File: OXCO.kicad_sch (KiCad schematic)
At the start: 18 parts, among them U4 LT1963AEQ, U7 ADR4540

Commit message: OCXO Rev. 0
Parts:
- added 2V1: TEST_VADJ, TestPoint:TestPoint_2Pads_Pitch2.54mm_Drill0.8mm, symbol Connector:TestPoint_2Pole
- added RV1: 2K, symbol Device:R_Potentiometer_Trim
- RN1: value R_Pack04 -> 1K 0.1% ±15ppm
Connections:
- net +5V: now also C15.1, C16.1, U5.5 (Vcc)
- net GND: now also C14.2, RN1.4 (R4.1), 2V1.2
- net Vadj: now also 2V1.1, RV1.2
- net at C11.1, C13.1, U7.6 (OUT): now also RN1.8 (R1.2)
- net at RN1.1 (R1.1): now also RN1.2 (R2.1)
- net at RN1.3 (R3.1): now also RV1.3
- net at RN1.5 (R4.2): now also RN1.6 (R3.2)
- net at RN1.7 (R2.2): now also RV1.1
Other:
- note added: "1.365V"
- note added: "3.000V"
- note added: "4.096V"
- note added: "ADR4540BRZ 2ppm/°C"
- note added: "ADR4540BRZ 4ppm/°C"
- note added: "OSC5AB02"
- moved on the sheet: 5V1, C1, C14, C15, C16, C2, D2, R1, R2, R3, U4, U5

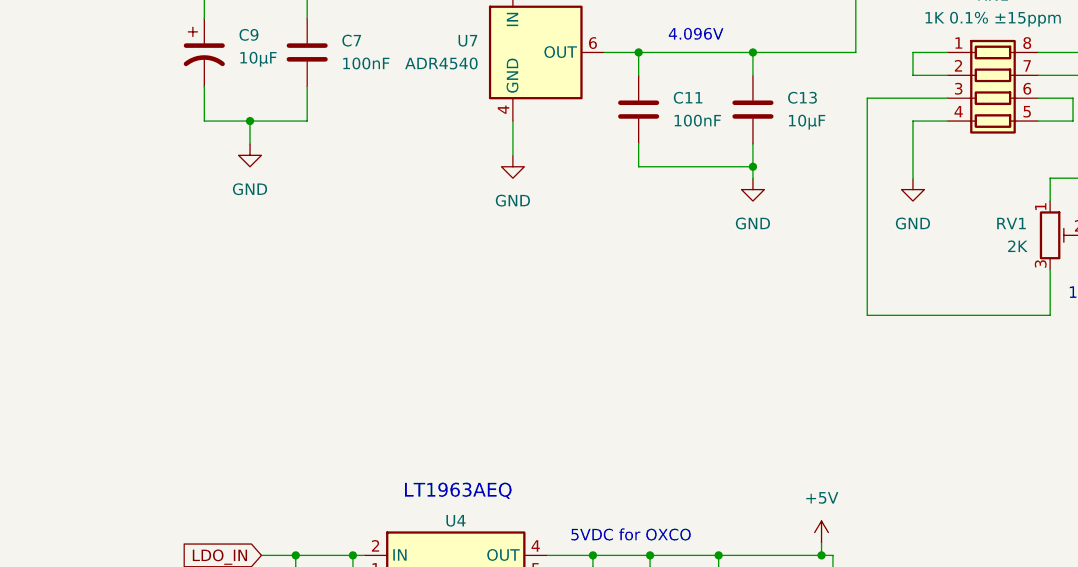
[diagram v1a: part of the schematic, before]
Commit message: Update OXCO.kicad_sch
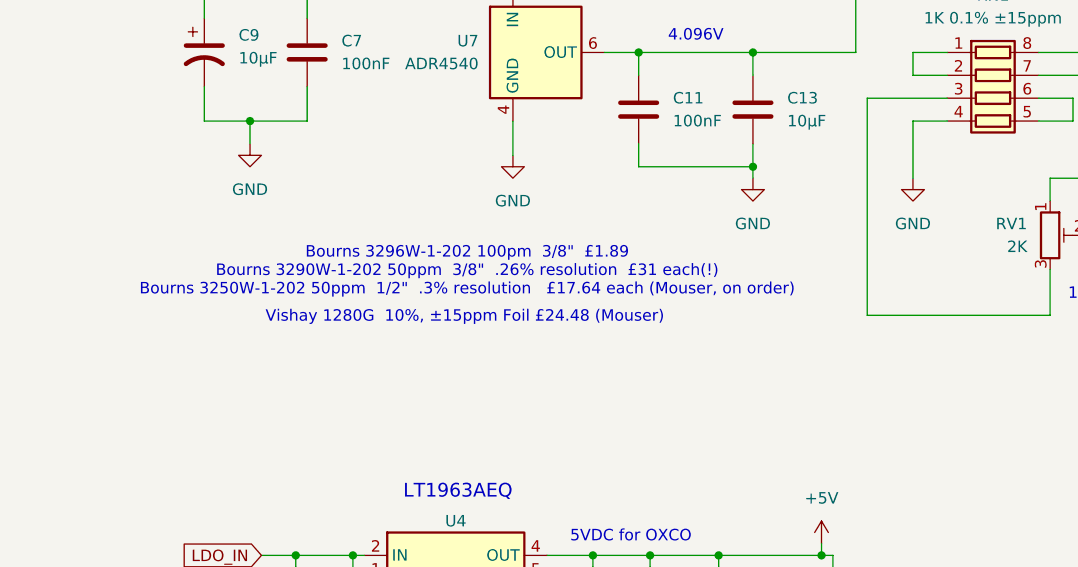
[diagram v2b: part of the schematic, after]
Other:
- note added: "Bourns 3296W-1-202 100pm 3/8" £1.89 Bourns 3290W-1-202 50ppm 3/8" .26% resolution £31 each(!) Bourns 3250W-1-202 50ppm 1/2" .3% resolution £17.64 each (Mouser, on order)"
- note added: "Vishay 1280G 10%, ±15ppm Foil £24.48 (Mouser)"
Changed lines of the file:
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@@
+		)
+	)
+	(text "Bourns 3296W-1-202 100pm  3/8\"  £1.89\nBourns 3290W-1-202 50ppm  3/8\"  .26% resolution  £31 each(!)\nBourns 3250W-1-202 50ppm  1/2\"  .3% resolution   £17.64 each (Mouser, on order)\n"
+		(exclude_from_sim no)
+		(at 60.96 94.234 0)
+		(effects
+			(font
+				(face "Arial")
+				(size 1.27 1.27)
+			)
 		)
 	)
@@
 		(effects
 			(font
+				(size 1.27 1.27)
+			)
+		)
+	)
+	(text "Vishay 1280G  10%, ±15ppm Foil £24.48 (Mouser) "
+		(exclude_from_sim no)
+		(at 60.706 99.314 0)
+		(effects
+			(font

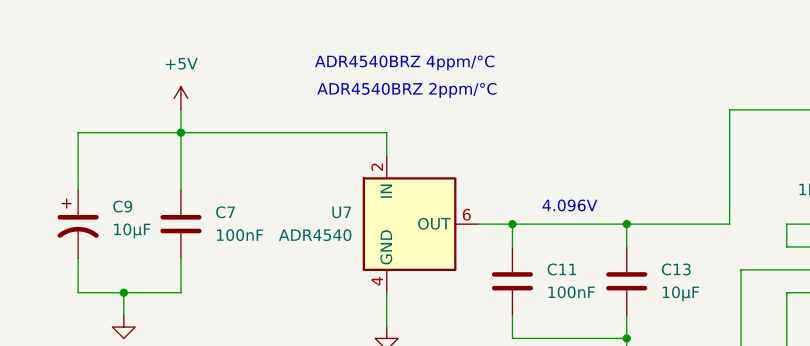
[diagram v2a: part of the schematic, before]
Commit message: Placeholder footprint for trimpot
also fix a typo
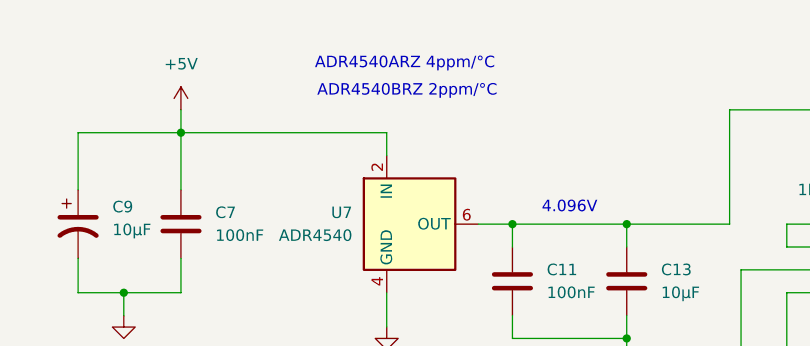
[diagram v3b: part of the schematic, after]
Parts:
- RV1: footprint (none) -> Potentiometer_THT:Potentiometer_Bourns_3296W_Vertical
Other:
- note added: "ADR4540ARZ 4ppm/°C"
- note removed: "ADR4540BRZ 4ppm/°C"
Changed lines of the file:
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@@
 		)
 	)
-	(text "ADR4540BRZ 4ppm/°C"
+	(text "ADR4540ARZ 4ppm/°C"
 		(exclude_from_sim no)
 		(at 68.072 52.07 0)
@@
 			)
 		)
-		(property "Footprint" ""
+		(property "Footprint" "Potentiometer_THT:Potentiometer_Bourns_3296W_Vertical"
 			(at 125.73 90.17 0)
 			(effects

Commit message: Add missing footprints
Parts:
- RN1: footprint (none) -> Resistor_SMD:R_Array_Convex_4x0612
- U5: footprint (none) -> Oscilator_Local:OSC5A2B02
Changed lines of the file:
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@@
 			)
 		)
-		(property "Footprint" ""
+		(property "Footprint" "Oscilator_Local:OSC5A2B02"
 			(at 194.31 63.5 0)
 			(effects
@@
 			)
 		)
-		(property "Footprint" ""
+		(property "Footprint" "Resistor_SMD:R_Array_Convex_4x0612"
 			(at 119.38 81.915 90)
 			(effects

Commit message: things
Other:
- note added: "Vishay 1280G has similar footprint as Bourn 3005P and 3006P. Possible to layout so all three fit. Be sure to import 3D files for all 3."
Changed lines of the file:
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@@
+		)
+	)
+	(text "Vishay 1280G has similar footprint as Bourn 3005P and 3006P.\nPossible to layout so all three fit.   Be sure to import 3D files for all 3.  "
+		(exclude_from_sim no)
+		(at 122.682 102.616 0)
+		(effects
+			(font
+				(size 1.27 1.27)
+			)
 		)
 	)

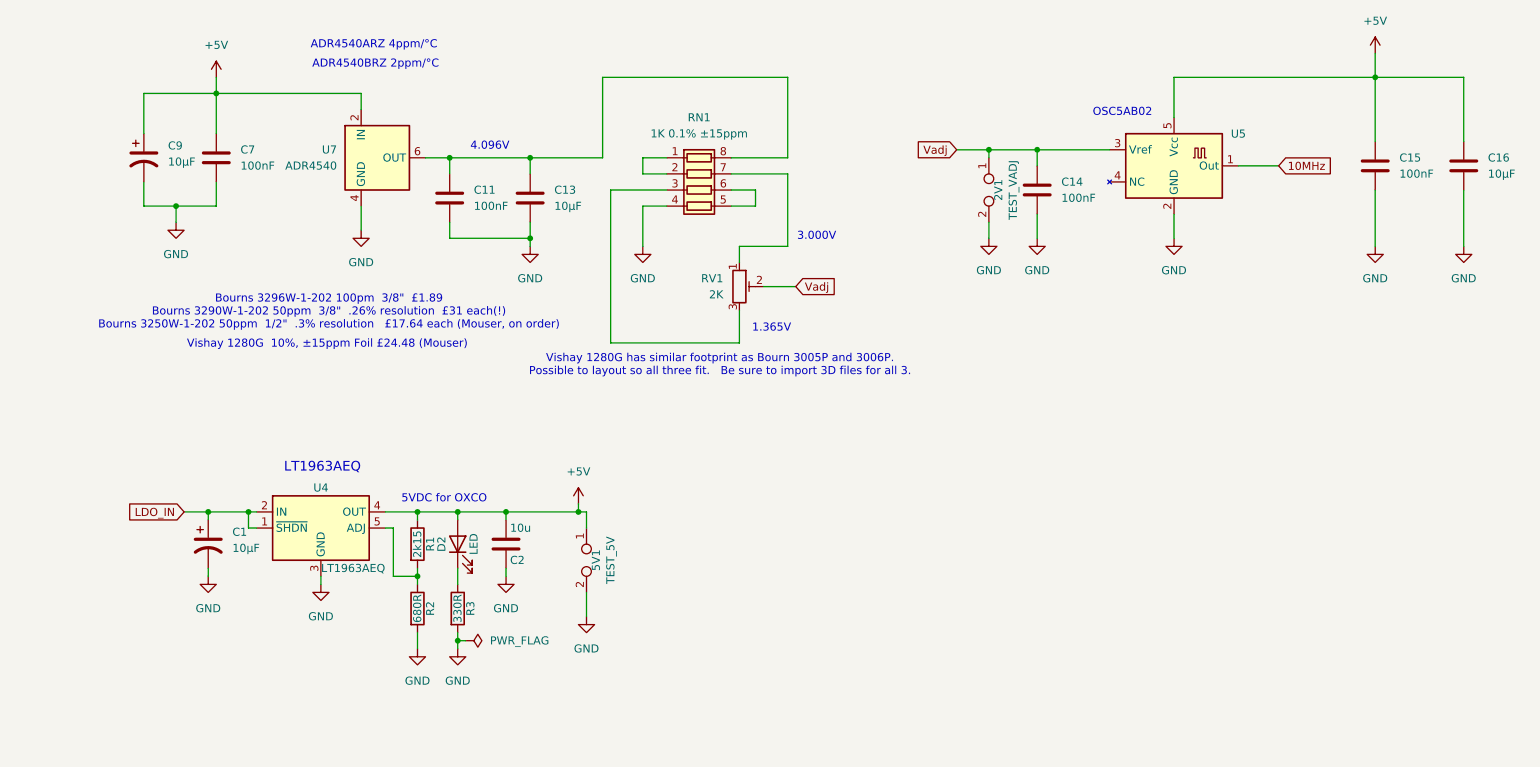
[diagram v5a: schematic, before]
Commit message: A bit of layout work
Remove sine to square parts from layout.  We don't need it.
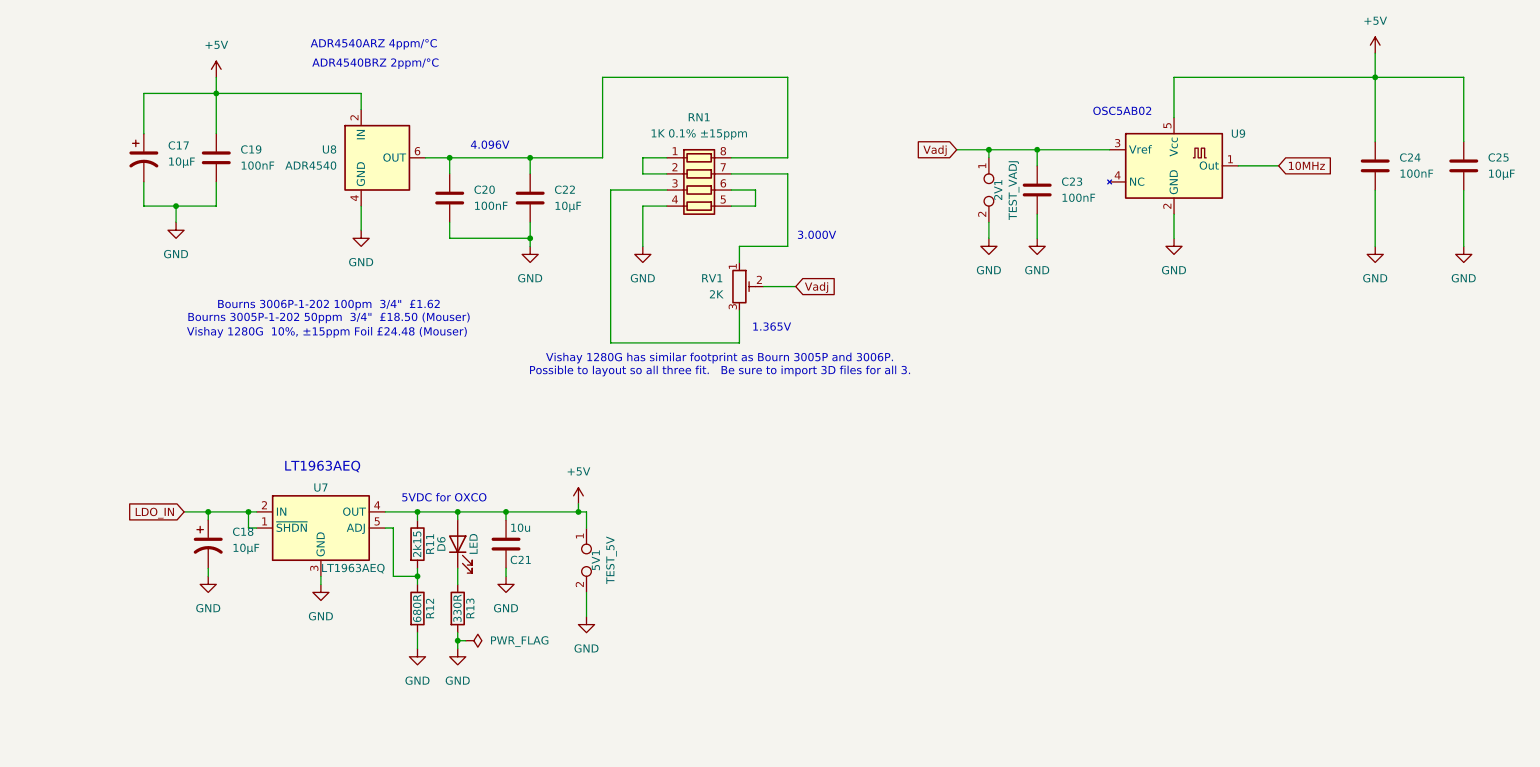
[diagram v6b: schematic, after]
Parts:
- RV1: footprint Potentiometer_THT:Potentiometer_Bourns_3296W_Vertical -> Potentiometer_THT:Potentiometer_Bourns_3006P_Horizontal; MPN (none) -> 3006P-1-202LF; RS (none) -> 521-9085
- renumbered C9 to C17, C1 to C18, C7 to C19, C11 to C20, C2 to C21, C13 to C22, C14 to C23, C15 to C24, C16 to C25, D2 to D6, R1 to R11, R2 to R12, R3 to R13, U4 to U7, U7 to U8, U5 to U9
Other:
- note added: "Bourns 3006P-1-202 100pm 3/4" £1.62 Bourns 3005P-1-202 50ppm 3/4" £18.50 (Mouser)"
- note removed: "Bourns 3296W-1-202 100pm 3/8" £1.89 Bourns 3290W-1-202 50ppm 3/8" .26% resolution £31 each(!) Bourns 3250W-1-202 50ppm 1/2" .3% resolution £17.64 each (Mouser, on order)"

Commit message: Redraw for clarity.   Add LCSC parts.
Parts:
- C21: LCSC (none) -> C15850; MPN (none) -> CL21A106KAYNNNE
- R11: LCSC (none) -> C865365; MPN (none) -> RT0805BRD072K15L
- R12: LCSC (none) -> C17798; MPN (none) -> 0805W8F6800T5E
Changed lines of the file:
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@@
 			)
 		)
-		(property "Description" "Resistor"
+		(property "Description" "1% 100ppm - Basic part"
 			(at 74.93 140.97 0)
+			(effects
+				(font
+					(size 1.27 1.27)
+				)
+				(hide yes)
+			)
+		)
+		(property "MPN" "0805W8F6800T5E"
+			(at 74.93 140.97 90)
+			(effects
+				(font
+					(size 1.27 1.27)
+				)
+				(hide yes)
+			)
+		)
+		(property "LCSC" "C17798"
+			(at 74.93 140.97 90)
 			(effects
 				(font
@@
 			)
 		)
+		(property "MPN" "CL21A106KAYNNNE"
+			(at 88.9 130.81 0)
+			(effects
+				(font
+					(size 1.27 1.27)
+				)
+				(hide yes)
+			)
+		)
+		(property "LCSC" "C15850"
+			(at 88.9 130.81 0)
+			(effects
+				(font
+					(size 1.27 1.27)
+				)
+				(hide yes)
+			)
+		)
 		(pin "1"
 		)
@@
 			)
 		)
-		(property "Description" "Resistor"
+		(property "Description" "2.15kΩ ±25ppm/℃ ±0.1%"
 			(at 74.93 130.81 0)
 			(effects
 				(font
+					(size 1.27 1.27)
+				)
+				(hide yes)
+			)
+		)
+		(property "MPN" "RT0805BRD072K15L"
+			(at 74.93 130.81 90)
+			(effects
+				(font
+					(size 1.27 1.27)
+				)
+				(hide yes)
+			)
+		)
+		(property "LCSC" "C865365"
+			(at 74.93 130.81 90)
+			(effects
+				(font

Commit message: layout
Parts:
- added C26: 100nF, Capacitor_SMD:C_0402_1005Metric_Pad0.74x0.62mm_HandSolder, symbol Device:C
- 2V1: value TEST_VADJ -> VADJ
- 5V1: value TEST_5V -> 5V
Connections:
- net GND: now also C26.2
- net Vadj: now also C26.1
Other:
- note added: "Vishay 1280G has similar footprint as Bourns 3005P and 3006P. Possible to layout so all three fit."
- note removed: "Vishay 1280G has similar footprint as Bourn 3005P and 3006P. Possible to layout so all three fit. Be sure to import 3D files for all 3."
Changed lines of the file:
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@@
 	)
 	(junction
+		(at 138.43 90.17)
+		(diameter 0)
+		(color 0 0 0 0)
+	)
+	(junction
 		(at 226.06 57.15)
 		(diameter 0)
@@
 	(wire
 		(pts
-			(xy 129.54 90.17) (xy 134.62 90.17)
+			(xy 129.54 90.17) (xy 138.43 90.17)
 		)
 		(stroke
@@
 	(wire
 		(pts
+			(xy 138.43 90.17) (xy 138.43 91.44)
+		)
+		(stroke
+			(width 0)
+			(type default)
+		)
+	)
+	(wire
+		(pts
 			(xy 80.01 69.85) (xy 92.71 69.85)
 		)
@@
 	(wire
 		(pts
+			(xy 138.43 99.06) (xy 138.43 101.6)
+		)
+		(stroke
+			(width 0)
+			(type default)
+		)
+	)
+	(wire
+		(pts
 			(xy 43.18 59.69) (xy 43.18 66.04)
 		)
@@
 	(wire
 		(pts
+			(xy 138.43 90.17) (xy 143.51 90.17)
+		)
+		(stroke
+			(width 0)
+			(type default)
+		)
+	)
+	(wire
+		(pts
 			(xy 105.41 99.06) (xy 125.73 99.06)
 		)
@@
 		)
 	)
-	(text "Vishay 1280G has similar footprint as Bourn 3005P and 3006P.\nPossible to layout so all three fit.   Be sure to import 3D files for all 3.  "
+	(text "Vishay 1280G has similar footprint as Bourns 3005P\n and 3006P. Possible to layout so all three fit. "
 		(exclude_from_sim no)
-		(at 122.682 102.616 0)
+		(at 127 110.49 0)
 		(effects
 			(font
@@
 	(global_label "Vadj"
 		(shape input)
-		(at 134.62 90.17 0)
+		(at 143.51 90.17 0)
 		(fields_autoplaced yes)
 		(effects
@@
 		)
 		(property "Intersheetrefs" "${INTERSHEET_REFS}"
-			(at 140.9424 90.17 0)
+			(at 149.8324 90.17 0)
 			(effects
 				(font
@@
 			)
 		)
-		(property "Value" "TEST_VADJ"
+		(property "Value" "VADJ"
 			(at 168.91 74.93 0)
 			(effects
@@
 	(symbol
 		(lib_id "power:GND")
+		(at 138.43 101.6 0)
+		(unit 1)
+		(exclude_from_sim no)
+		(in_bom yes)
+		(on_board yes)
+		(dnp no)
+		(fields_autoplaced yes)
+		(property "Reference" "#PWR023"
+			(at 138.43 107.95 0)
+			(effects
+				(font
+					(size 1.27 1.27)
+				)
+				(hide yes)
+			)
+		)
+		(property "Value" "GND"
+			(at 138.43 106.68 0)
+			(effects
+				(font
+					(size 1.27 1.27)
+				)
+			)
+		)
+		(property "Footprint" ""
+			(at 138.43 101.6 0)
+			(effects
+				(font
+					(size 1.27 1.27)
+				)
+				(hide yes)
+			)
+		)
+		(property "Datasheet" ""
+			(at 138.43 101.6 0)
+			(effects
+				(font
+					(size 1.27 1.27)
+				)
+				(hide yes)
+			)
+		)
+		(property "Description" "Power symbol creates a global label with name \"GND\" , ground"
+			(at 138.43 101.6 0)
+			(effects
+				(font
+					(size 1.27 1.27)
+				)
+				(hide yes)
+			)
+		)
+		(pin "1"
+		)
+		(instances
+			(project ""
+				(path "/eba36321-b5f3-4bd6-a805-57b9b2ee447e/e769b68a-585d-4de6-8d1e-4dcee65d99b9"
+					(reference "#PWR023")
+					(unit 1)
+				)
+			)
+		)
+	)
+	(symbol
+		(lib_id "power:GND")
 		(at 59.69 137.16 0)
 		(unit 1)
@@
 	)
 	(symbol
+		(lib_id "Device:C")
+		(at 138.43 95.25 0)
+		(unit 1)
+		(exclude_from_sim no)
+		(in_bom yes)
+		(on_board yes)
+		(dnp no)
+		(fields_autoplaced yes)
+		(property "Reference" "C26"
+			(at 142.24 93.9799 0)
+			(effects
+				(font
+					(size 1.27 1.27)
+				)
+				(justify left)
+			)
+		)
+		(property "Value" "100nF"
+			(at 142.24 96.5199 0)
+			(effects
+				(font
+					(size 1.27 1.27)
+				)
+				(justify left)
+			)
+		)
+		(property "Footprint" "Capacitor_SMD:C_0402_1005Metric_Pad0.74x0.62mm_HandSolder"
+			(at 139.3952 99.06 0)
+			(effects
+				(font
+					(size 1.27 1.27)
+				)
+				(hide yes)
+			)
+		)
+		(property "Datasheet" "~"
+			(at 138.43 95.25 0)
+			(effects
+				(font
+					(size 1.27 1.27)
+				)
+				(hide yes)
+			)
+		)
+		(property "Description" "Unpolarized capacitor"
+			(at 138.43 95.25 0)
+			(effects
+				(font
+					(size 1.27 1.27)
+				)
+				(hide yes)
+			)
+		)
+		(property "LCSC" "C1525"
+			(at 138.43 95.25 0)
+			(effects
+				(font
+					(size 1.27 1.27)
+				)
+				(hide yes)
+			)
+		)
+		(property "MPN" "CL05B104KO5NNNC "
+			(at 138.43 95.25 0)
+			(effects
+				(font
+					(size 1.27 1.27)
+				)
+				(hide yes)
+			)
+		)
+		(pin "2"
+		)
+		(pin "1"
+		)
+		(instances
+			(project "picdiv_board_v4AF"
+				(path "/eba36321-b5f3-4bd6-a805-57b9b2ee447e/e769b68a-585d-4de6-8d1e-4dcee65d99b9"
+					(reference "C26")
+					(unit 1)
+				)
+			)
+		)
+	)
+	(symbol
 		(lib_id "power:GND")
 		(at 41.91 135.89 0)
@@
 			)
 		)
-		(property "Value" "TEST_5V"
+		(property "Value" "5V"
 			(at 105.41 133.35 0)
 			(effects
